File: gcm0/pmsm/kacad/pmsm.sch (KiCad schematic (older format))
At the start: 65 parts, among them U5 STM32F030F4P6, U9 74HC595, Y1 8M

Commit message: 电路图
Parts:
- removed C? (x4): 104, symbol Device:C
- removed C? (x4): 100UF, symbol Device:CP
- removed Q?: Q_PNP_BCE, symbol Device:Q_PNP_BCE
- removed R? (x3): 100, symbol Device:R
- removed R? (x9): 1K, symbol Device:R
- removed R? (x2): 20K, symbol Device:R
- removed U?: LM317_TO-220, Package_TO_SOT_THT:TO-220-3_Vertical, symbol Regulator_Linear:LM317_TO-220
- removed U? (x3): NE5532, symbol Amplifier_Operational:NE5532
- added C1, C2: 105, symbol Device:C
- added C10, C11, C23, C6, C8, C9: 104, symbol Device:C
- added C12, C5, C7: 100UF, symbol Device:CP
- added C13: 1000UF, symbol Device:CP
- added C3, C4: 102, symbol Device:C
- added D1: 1N4007, Diode_THT:D_DO-41_SOD81_P10.16mm_Horizontal, symbol Diode:1N4007
- added D2: 1N5822, Diode_THT:D_DO-201AD_P15.24mm_Horizontal, symbol Diode:1N5822
- added J1: +12, symbol Connector:Conn_01x01_Male
- added J10: SIN-, symbol Connector:Conn_01x01_Male
- added J2: dian_ji_shu_chu_a, symbol Connector:Conn_01x01_Male
- added J3: chuan_gan_qi_shu_chu+, symbol Connector:Conn_01x01_Male
- added J4: chuan_gan_qi_shu_chu-, symbol Connector:Conn_01x01_Male
- added J5: dian_ji_shu_chu_b, symbol Connector:Conn_01x01_Male
- added J6: dian_ji_shu_chu_c, symbol Connector:Conn_01x01_Male
- added J7: COS-, symbol Connector:Conn_01x01_Male
- added J8: COS+, symbol Connector:Conn_01x01_Male
- added J9: SIN+, symbol Connector:Conn_01x01_Male
- added J? (x2): GND, symbol Connector:Conn_01x01_Male
- added J?: SWD, symbol Connector:Conn_01x03_Male
- added L1: 100UH, symbol Device:L_Core_Iron
- added L2: 47UH, symbol Device:L_Core_Iron
- added Q1, Q11, Q8: BC547, Package_TO_SOT_THT:TO-92_Inline, symbol Transistor_BJT:BC547
- added Q10, Q13, Q3: TIP127, Package_TO_SOT_THT:TO-220-3_Vertical, symbol Transistor_BJT:TIP127
- added Q12, Q2, Q9: TIP122, Package_TO_SOT_THT:TO-220-3_Vertical, symbol Transistor_BJT:TIP122
- added Q4, Q6: SS8550, symbol Transistor_BJT:S8550
- added Q5, Q7: SS8050, symbol Transistor_BJT:S8050
- added R1, R11, R16, R18, R20, R21, R23, R24, R3, R4, R7, R8: 1K, symbol Device:R
- added R10, R13, R2, R22, R9: 100, symbol Device:R
- added R19: 250, symbol Device:R
- added R5, R6: 100K, symbol Device:R
- added U1: LM7809_TO220, Package_TO_SOT_THT:TO-220-3_Vertical, symbol Regulator_Linear:LM7809_TO220
- added U3: LM7805_TO220, Package_TO_SOT_THT:TO-220-3_Vertical, symbol Regulator_Linear:LM7805_TO220
- added U4: LM2576T-ADJ, Package_TO_SOT_THT:TO-220-5_Vertical, symbol Regulator_Switching:LM2576T-ADJ
- C18: renamed from C?; value 104 -> 105
- C19, C20, C21, C22: renamed from C?; value C -> 104
- R25, R26, R28, R30: renamed from R?; value R -> 5K
- R29: value 1K -> 1.5K
- R31, R32: renamed from R?; value R -> 100K
- R35, R36: renamed from R?; value R -> 100
- gave numbers to parts that had none: 8
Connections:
- net labels added: +5V, +9V, -5V, CLK, DIO, PA6_TIM3_PWM_CH1, PA7_TIM3_PWM_CH2, PA9_TIM1_PWM_CH2
- net labels removed: +10V, GNDREF
- wire segments 202 -> 305
- no-connect marks 2 -> 8
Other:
- note added: "chuan_gan_qi_ji_li"
- note added: "dian_ji_qu_dong"
- moved on the sheet: C14, C15, C16, C17, C18, C19, C20, C21, C22, DS1, R12, R14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

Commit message: 让电机转
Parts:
- removed D1: 1N4007, Diode_THT:D_DO-41_SOD81_P10.16mm_Horizontal, symbol Diode:1N4007
- gave numbers to parts that had none: 3
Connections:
- net labels added: PA4_TIM14_PWM_CH1, PA5_ADC5_SIN
- net labels removed: PA4_ADC4_SIN, PA9_TIM1_PWM_CH2
- wire segments 305 -> 299
- no-connect marks 8 -> 7
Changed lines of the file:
@@
 L power:GND #PWR0103
 U 1 1 6083D183
-P 2100 10750
-F 0 "#PWR0103" H 2100 10500 50  0001 C CNN
-F 1 "GND" H 2105 10577 50  0000 C CNN
-F 2 "" H 2100 10750 50  0001 C CNN
-F 3 "" H 2100 10750 50  0001 C CNN
-	1    2100 10750
+P 1450 9750
+F 0 "#PWR0103" H 1450 9500 50  0001 C CNN
+F 1 "GND" H 1455 9577 50  0000 C CNN
+F 2 "" H 1450 9750 50  0001 C CNN
+F 3 "" H 1450 9750 50  0001 C CNN
+	1    1450 9750
 	1    0    0    -1
 $EndComp
@@
 L power:PWR_FLAG #FLG0101
 U 1 1 6083DEC9
-P 2100 10750
-F 0 "#FLG0101" H 2100 10825 50  0001 C CNN
-F 1 "PWR_FLAG" H 2100 10923 50  0000 C CNN
-F 2 "" H 2100 10750 50  0001 C CNN
-F 3 "~" H 2100 10750 50  0001 C CNN
-	1    2100 10750
+P 1450 9750
+F 0 "#FLG0101" H 1450 9825 50  0001 C CNN
+F 1 "PWR_FLAG" H 1450 9923 50  0000 C CNN
+F 2 "" H 1450 9750 50  0001 C CNN
+F 3 "~" H 1450 9750 50  0001 C CNN
+	1    1450 9750
 	1    0    0    -1
 $EndComp
@@
 L power:PWR_FLAG #FLG0102
 U 1 1 6083F6EE
-P 1650 10750
-F 0 "#FLG0102" H 1650 10825 50  0001 C CNN
-F 1 "PWR_FLAG" H 1650 10923 50  0000 C CNN
-F 2 "" H 1650 10750 50  0001 C CNN
-F 3 "~" H 1650 10750 50  0001 C CNN
-	1    1650 10750
+P 1000 9750
+F 0 "#FLG0102" H 1000 9825 50  0001 C CNN
+F 1 "PWR_FLAG" H 1000 9923 50  0000 C CNN
+F 2 "" H 1000 9750 50  0001 C CNN
+F 3 "~" H 1000 9750 50  0001 C CNN
+	1    1000 9750
 	-1   0    0    1
 $EndComp
@@
 L power:+12V #PWR0104
 U 1 1 6083FFF0
-P 1650 10750
-F 0 "#PWR0104" H 1650 10600 50  0001 C CNN
-F 1 "+12V" H 1665 10923 50  0000 C CNN
-F 2 "" H 1650 10750 50  0001 C CNN
-F 3 "" H 1650 10750 50  0001 C CNN
-	1    1650 10750
+P 1000 9750
+F 0 "#PWR0104" H 1000 9600 50  0001 C CNN
+F 1 "+12V" H 1015 9923 50  0000 C CNN
+F 2 "" H 1000 9750 50  0001 C CNN
+F 3 "" H 1000 9750 50  0001 C CNN
+	1    1000 9750
 	1    0    0    -1
 $EndComp
@@
 Wire Wire Line
 	8100 5800 8100 6500
-Wire Wire Line
-	8100 6500 10150 6500
 $Comp
 L Amplifier_Operational:TL084 U7
@@
 Wire Wire Line
 	14650 8800 14900 8800
-Wire Wire Line
-	11250 2450 10800 2450
-Connection ~ 11250 2450
-Text Label 10800 2450 0    50   ~ 0
+Text Label 11000 2450 2    50   ~ 0
 PA6_RCLK
 Wire Wire Line
@@
 Wire Wire Line
 	11950 2150 11950 2350
-Wire Wire Line
-	11950 2350 11500 2350
 Connection ~ 11950 2150
 Wire Wire Line
 	11950 2150 12300 2150
-Text Label 11500 2350 0    50   ~ 0
+Text Label 11850 2350 2    50   ~ 0
 PA5_SRCLK
 Wire Wire Line
@@
 	12950 1600 14450 1600
 Connection ~ 14450 1600
-Wire Wire Line
-	12150 1600 11750 1600
-Text Label 11800 1600 0    50   ~ 0
+Text Label 12150 1600 0    50   ~ 0
 PA7_SER
-Text Label 9550 4800 0    50   ~ 0
+Text Label 9450 4800 0    50   ~ 0
 PA6_RCLK
-Text Label 9550 4900 0    50   ~ 0
+Text Label 9450 4900 0    50   ~ 0
 PA7_SER
-Text Label 9550 4700 0    50   ~ 0
+Text Label 9450 4700 0    50   ~ 0
 PA5_SRCLK
-Wire Wire Line
-	9350 4700 10000 4700
-Wire Wire Line
-	9350 4800 10000 4800
-Wire Wire Line
-	9350 4900 10000 4900
-Text Label 15600 7950 2    50   ~ 0
+Text Label 15100 7950 0    50   ~ 0
 PA3_ADC3_COS
-Wire Wire Line
-	14950 7950 15600 7950
-Connection ~ 14950 7950
-Text Label 15600 8800 2    50   ~ 0
-PA4_ADC4_SIN
-Text Label 9450 5100 0    50   ~ 0
-PA4_ADC4_SIN
+Text Label 15150 8800 0    50   ~ 0
+PA5_ADC5_SIN
+Text Label 9450 5200 0    50   ~ 0
+PA5_ADC5_SIN
 Text Label 9450 5000 0    50   ~ 0
 PA3_ADC3_COS
-Wire Wire Line
-	14900 8800 15650 8800
-Connection ~ 14900 8800
 Wire Wire Line
 	12000 7600 11500 7600
@@
 Wire Wire Line
 	15050 6750 15200 6750
-Wire Wire Line
-	9350 5000 10000 5000
-Wire Wire Line
-	9350 5100 10000 5100
 Text Label 9450 5600 0    50   ~ 0
 PA10_SPWM_Resolver+
-Text Label 9200 6500 0    50   ~ 0
+Text Label 8100 6500 0    50   ~ 0
 PB1_SPWM_Resolver-
-Text Label 1200 4400 0    50   ~ 0
+Text Label 2000 4400 2    50   ~ 0
 PA10_SPWM_Resolver+
-Text Label 1200 5900 0    50   ~ 0
+Text Label 2050 5900 2    50   ~ 0
 PB1_SPWM_Resolver-
 $Comp
@@
 $EndComp
 $Comp
-L Diode:1N4007 D1
-U 1 1 60D5A099
-P 2000 8350
-F 0 "D1" H 2000 8133 50  0000 C CNN
-F 1 "1N4007" H 2000 8224 50  0000 C CNN
-F 2 "Diode_THT:D_DO-41_SOD81_P10.16mm_Horizontal" H 2000 8175 50  0001 C CNN
-F 3 "http://www.vishay.com/docs/88503/1n4001.pdf" H 2000 8350 50  0001 C CNN
-	1    2000 8350
-	-1   0    0    1
-$EndComp
-$Comp
 L power:+5V #PWR0126
 U 1 1 60D5D5A3
@@
 	1    0    0    -1
 $EndComp
-Wire Wire Line
-	9350 5600 10300 5600
-Wire Wire Line
-	2000 4400 1200 4400
-Wire Wire Line
-	2050 5900 1200 5900
 $Comp
 L Connector:Conn_01x01_Male J1
@@
 	1    0    0    -1
 $EndComp
-Wire Wire Line
-	1600 8350 1850 8350
 $Comp
 L Connector:Conn_01x01_Male J3
@@
 Wire Wire Line
 	2900 2150 2500 2150
-Wire Wire Line
-	9350 5300 10250 5300
-Wire Wire Line
-	9350 5400 10250 5400
-Wire Wire Line
-	9350 5500 10250 5500
 Text Label 9450 5300 0    50   ~ 0
 PA6_TIM3_PWM_CH1
 Text Label 9450 5400 0    50   ~ 0
 PA7_TIM3_PWM_CH2
-Text Label 9450 5500 0    50   ~ 0
-PA9_TIM1_PWM_CH2
-Text Label 1400 3350 0    50   ~ 0
+Text Label 9450 5100 0    50   ~ 0
+PA4_TIM14_PWM_CH1
+Text Label 1100 3100 0    50   ~ 0
 PA6_TIM3_PWM_CH1
-Text Label 3250 2650 0    50   ~ 0
+Text Label 4050 2650 2    50   ~ 0
 PA7_TIM3_PWM_CH2
-Text Label 6150 2750 0    50   ~ 0
-PA9_TIM1_PWM_CH2
 Connection ~ 2500 2150
 Wire Wire Line
@@
 	7600 2950 5650 2950
 Wire Wire Line
-	900  2400 900  3350
-Wire Wire Line
-	900  3350 2200 3350
-Wire Wire Line
 	4050 2400 4050 2650
 Wire Wire Line
-	4050 2650 3250 2650
-Wire Wire Line
 	7000 2400 7000 2750
-Wire Wire Line
-	6150 2750 7000 2750
 Wire Wire Line
 	2800 5900 2850 5900
@@
 NoConn ~ 14050 2500
 NoConn ~ 14050 2600
-NoConn ~ 9350 5200
 $Comp
 L Device:L_Core_Iron L2
@@
 Wire Wire Line
 	8950 4350 8950 4500
-Connection ~ 2150 8350
 Connection ~ 2350 8350
 Wire Wire Line
@@
 	2400 5550 2400 5900
 $Comp
-L Connector:Conn_01x01_Male J?
+L Connector:Conn_01x01_Male J12
 U 1 1 6228A4B7
 P 11300 8050
-F 0 "J?" H 11408 8231 50  0000 C CNN
+F 0 "J12" H 11408 8231 50  0000 C CNN
 F 1 "GND" H 11408 8140 50  0000 C CNN
 F 2 "" H 11300 8050 50  0001 C CNN
@@
 $EndComp
 $Comp
-L Connector:Conn_01x01_Male J?
+L Connector:Conn_01x01_Male J13
 U 1 1 6228C3BB
 P 11300 8600
-F 0 "J?" H 11408 8781 50  0000 C CNN
+F 0 "J13" H 11408 8781 50  0000 C CNN
 F 1 "GND" H 11408 8690 50  0000 C CNN
 F 2 "" H 11300 8600 50  0001 C CNN
@@
 	9350 5800 9950 5800
 $Comp
-L Connector:Conn_01x03_Male J?
+L Connector:Conn_01x03_Male J11
 U 1 1 6239EECD
 P 10150 5800
-F 0 "J?" H 10122 5732 50  0000 R CNN
+F 0 "J11" H 10122 5732 50  0000 R CNN
 F 1 "SWD" H 10122 5823 50  0000 R CNN
 F 2 "" H 10150 5800 50  0001 C CNN
@@
 $EndComp
 $Comp
-L power:GND #PWR?
+L power:GND #PWR03
 U 1 1 623A1478
 P 9950 5900
-F 0 "#PWR?" H 9950 5650 50  0001 C CNN
+F 0 "#PWR03" H 9950 5650 50  0001 C CNN
 F 1 "GND" H 9955 5727 50  0000 C CNN
 F 2 "" H 9950 5900 50  0001 C CNN
@@
 CLK
 $Comp
-L power:+9V #PWR?
+L power:+9V #PWR01
 U 1 1 623A535E
 P 3850 1500
-F 0 "#PWR?" H 3850 1350 50  0001 C CNN
+F 0 "#PWR01" H 3850 1350 50  0001 C CNN
 F 1 "+9V" H 3865 1673 50  0000 C CNN
 F 2 "" H 3850 1500 50  0001 C CNN
@@
 	3850 1500 4650 1500
 $Comp
-L power:GND #PWR?
+L power:GND #PWR02
 U 1 1 623A7D8D
 P 4000 2950
-F 0 "#PWR?" H 4000 2700 50  0001 C CNN
+F 0 "#PWR02" H 4000 2700 50  0001 C CNN
 F 1 "GND" H 4005 2777 50  0000 C CNN
 F 2 "" H 4000 2950 50  0001 C CNN
@@
 Wire Wire Line
 	4000 2950 2500 2950
+Text Label 7000 2750 2    50   ~ 0
+PA4_TIM14_PWM_CH1
+Wire Wire Line
+	1600 8350 2150 8350
+Connection ~ 2150 8350
+Wire Wire Line
+	11250 2450 11000 2450
+Connection ~ 11250 2450
+Wire Wire Line
+	11950 2350 11850 2350
+Wire Wire Line
+	900  2400 900  3100
+Wire Wire Line
+	900  3100 1100 3100
+Wire Wire Line
+	14950 7950 15100 7950
+Connection ~ 14950 7950
+Wire Wire Line
+	14900 8800 15150 8800
+Connection ~ 14900 8800
+Wire Wire Line
+	9350 4700 9450 4700
+Wire Wire Line
+	9350 4800 9450 4800
+Wire Wire Line
+	9350 4900 9450 4900
+Wire Wire Line
+	9350 5000 9450 5000
+Wire Wire Line
+	9350 5100 9450 5100
+Wire Wire Line
+	9350 5200 9450 5200
+Wire Wire Line
+	9350 5300 9450 5300
+Wire Wire Line
+	9350 5400 9450 5400
+Wire Wire Line
+	9350 5600 9450 5600
 $EndSCHEMATC

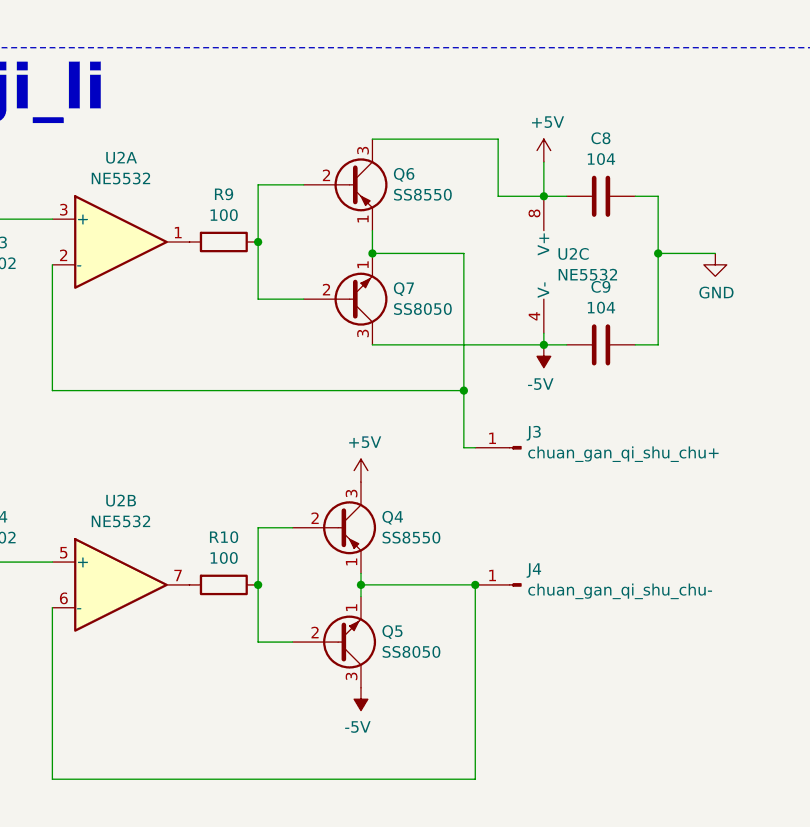
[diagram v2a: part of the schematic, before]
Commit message: 电路改错
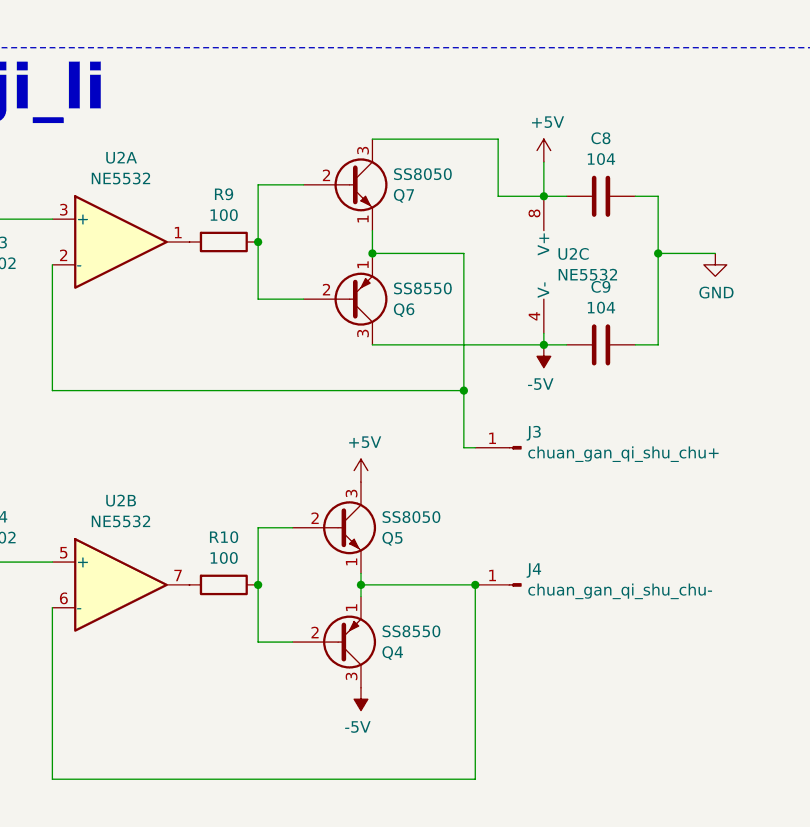
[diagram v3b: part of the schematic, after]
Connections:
- net +5V: now also Q5.3 (C), Q7.3 (C); no longer Q4.3 (C), Q6.3 (C)
- net -5V: now also Q4.3 (C), Q6.3 (C); no longer Q5.3 (C), Q7.3 (C)
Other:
- moved on the sheet: Q4, Q5, Q6, Q7
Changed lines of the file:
@@
 L Transistor_BJT:S8550 Q6
 U 1 1 60920E1B
-P 4550 4250
-F 0 "Q6" H 4740 4296 50  0000 L CNN
-F 1 "SS8550" H 4740 4205 50  0000 L CNN
-F 2 "" H 4750 4175 50  0001 L CIN
-F 3 "" H 4550 4250 50  0001 L CNN
-	1    4550 4250
-	1    0    0    -1
-$EndComp
-$Comp
-L Transistor_BJT:S8050 Q7
-U 1 1 60923A46
 P 4550 4750
-F 0 "Q7" H 4740 4704 50  0000 L CNN
-F 1 "SS8050" H 4740 4795 50  0000 L CNN
+F 0 "Q6" H 4740 4796 50  0000 L CNN
+F 1 "SS8550" H 4740 4705 50  0000 L CNN
 F 2 "" H 4750 4675 50  0001 L CIN
 F 3 "" H 4550 4750 50  0001 L CNN
@@
 $EndComp
 $Comp
+L Transistor_BJT:S8050 Q7
+U 1 1 60923A46
+P 4550 4250
+F 0 "Q7" H 4740 4204 50  0000 L CNN
+F 1 "SS8050" H 4740 4295 50  0000 L CNN
+F 2 "" H 4750 4175 50  0001 L CIN
+F 3 "" H 4550 4250 50  0001 L CNN
+	1    4550 4250
+	1    0    0    -1
+$EndComp
+$Comp
 L Transistor_BJT:S8550 Q4
 U 1 1 60935ADA
-P 4500 5750
-F 0 "Q4" H 4690 5796 50  0000 L CNN
-F 1 "SS8550" H 4690 5705 50  0000 L CNN
-F 2 "" H 4700 5675 50  0001 L CIN
-F 3 "" H 4500 5750 50  0001 L CNN
-	1    4500 5750
-	1    0    0    -1
-$EndComp
-$Comp
-L Transistor_BJT:S8050 Q5
-U 1 1 60935AE0
 P 4500 6250
-F 0 "Q5" H 4690 6204 50  0000 L CNN
-F 1 "SS8050" H 4690 6295 50  0000 L CNN
+F 0 "Q4" H 4690 6296 50  0000 L CNN
+F 1 "SS8550" H 4690 6205 50  0000 L CNN
 F 2 "" H 4700 6175 50  0001 L CIN
 F 3 "" H 4500 6250 50  0001 L CNN
 	1    4500 6250
 	1    0    0    1
+$EndComp
+$Comp
+L Transistor_BJT:S8050 Q5
+U 1 1 60935AE0
+P 4500 5750
+F 0 "Q5" H 4690 5704 50  0000 L CNN
+F 1 "SS8050" H 4690 5795 50  0000 L CNN
+F 2 "" H 4700 5675 50  0001 L CIN
+F 3 "" H 4500 5750 50  0001 L CNN
+	1    4500 5750
+	1    0    0    -1
 $EndComp
 Wire Wire Line
@@
 	3250 4600 3250 5150
 Wire Wire Line
-	3250 5150 5050 5150
-Wire Wire Line
 	5050 5150 5050 4550
 Wire Wire Line
@@
 Wire Wire Line
 	4650 4450 4650 4550
-Connection ~ 4650 4550
 Wire Wire Line
 	4650 4950 5400 4950
@@
 Wire Wire Line
 	9350 5600 9450 5600
+Connection ~ 4650 4550
+Wire Wire Line
+	3250 5150 5050 5150
 $EndSCHEMATC
